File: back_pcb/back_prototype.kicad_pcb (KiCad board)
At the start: 2 copper layers, 40 x 100 mm, 82 parts, among them P1 EXPANSION_LEFT, P2 EXPANSION_BOTTOM, P3 EXPANSION_TOP, P4 USB_A, P5 AUDIO_CONN, P6 ATMEGA_HEADER, P7 EXPANSION_BOTTOM2, P8 JST, P9 USB_A, Q1 IRLML6401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

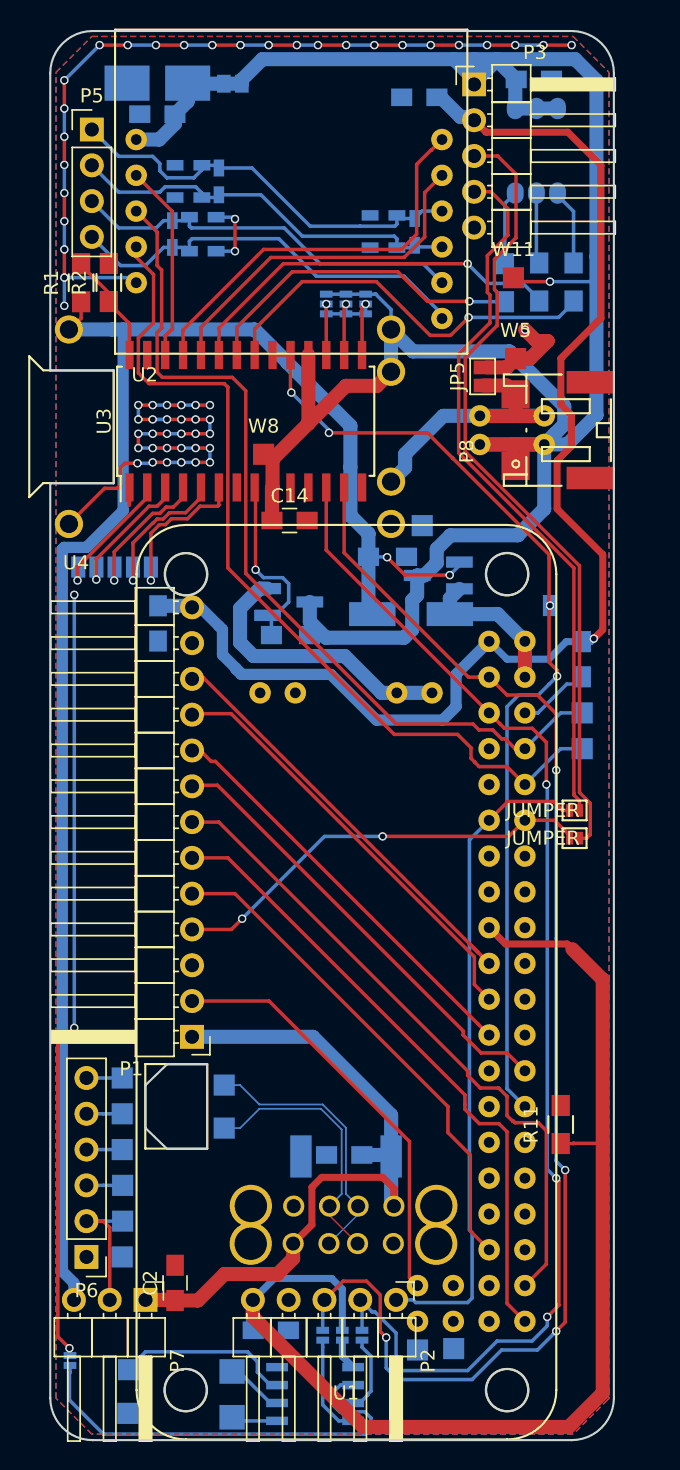
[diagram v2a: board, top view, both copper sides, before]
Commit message: Cleared up ground, removed testpoints
Removed some ground and I2C GPIO expander testpoints
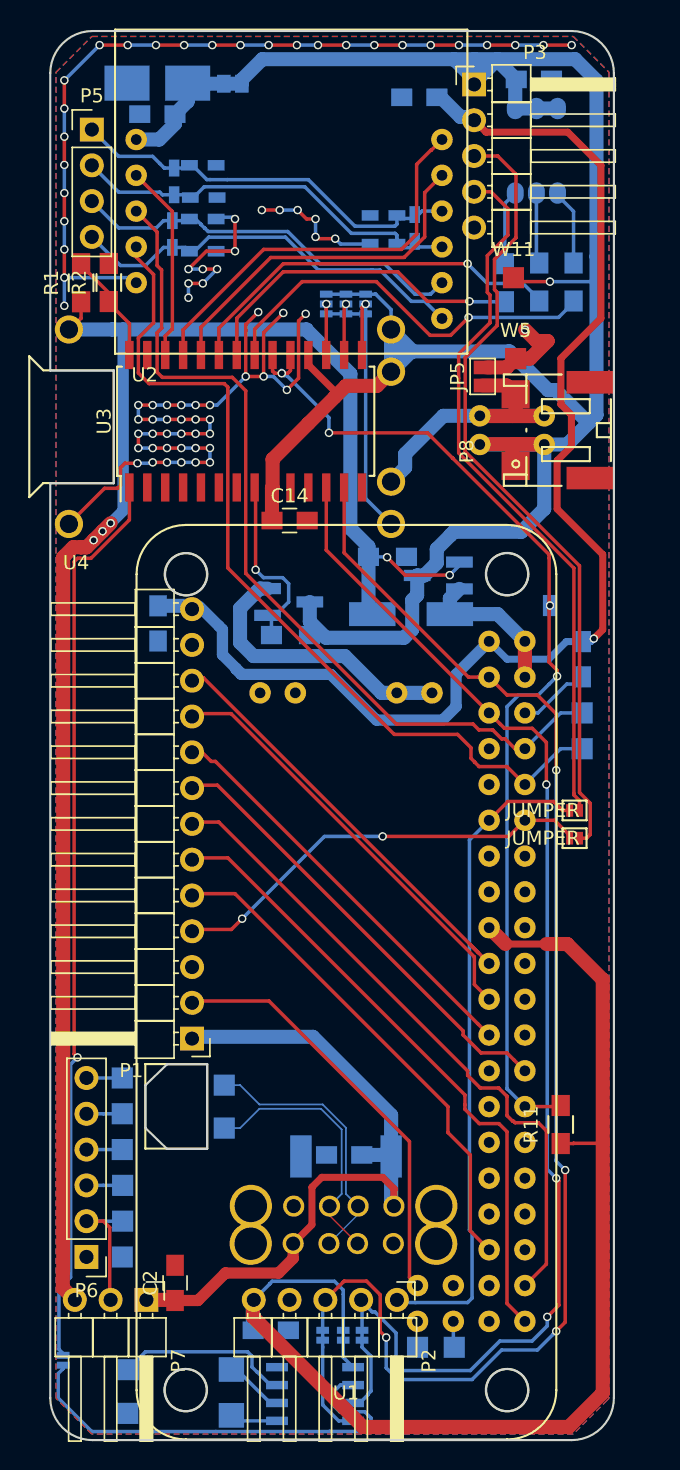
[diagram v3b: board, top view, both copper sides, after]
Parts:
- removed W12: GND, Measurement_Points:Measurement_Point_Square-SMD-Pad_Small
- removed W21, W22, W23, W24, W7, W8: TEST_1P, Measurement_Points:Measurement_Point_Square-SMD-Pad_Small
- moved C23 3.17 mm to (50.3, 50.7)
- moved C22 1.08 mm to (52.4, 51.8), turned to 180 degrees
- moved C24 1.02 mm to (52.3, 49.5), turned to 0 degrees
- moved JP2 0.48 mm to (42.4, 134.0)
- moved C17 0.28 mm to (67.4, 54.0)
- moved C16 0.25 mm to (65.2, 55.1)
- moved W4 0.19 mm to (67.6, 133.4)
- moved Y1 0.15 mm to (54.4, 136.6)
- moved C21 0.13 mm to (52.3, 53.3)
- moved P1 0.13 mm to (51.6, 111.5)
- moved W3 0.10 mm to (70.2, 133.4)
- moved JP7 0.06 mm to (62.3, 132.2)
- moved P7 0.06 mm to (48.3, 130.0)
- moved P2 0.06 mm to (66.1, 130.0)
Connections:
- JP10 pad 1: Net-(JP10-Pad1) -> SDA
- JP2 pad 1: Net-(JP2-Pad1) -> RTC_ALARM
- JP7 pad 1: Net-(JP7-Pad1) -> +3V3
- JP9 pad 1: Net-(JP9-Pad1) -> SCL
- U3 pad 2: Net-(U3-Pad2) -> (no net)
- U3 pad 3: Net-(U3-Pad3) -> (no net)
- U3 pad 4: Net-(U3-Pad4) -> (no net)
- U3 pad 5: Net-(U3-Pad5) -> (no net)
- U3 pad 6: Net-(U3-Pad6) -> (no net)
- U3 pad 7: Net-(U3-Pad7) -> (no net)
- U5 pad 5: Net-(JP7-Pad1) -> +3V3
- U5 pad 6: Net-(JP2-Pad1) -> RTC_ALARM
- U5 pad 7: Net-(JP9-Pad1) -> SCL
- U5 pad 8: Net-(JP10-Pad1) -> SDA
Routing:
- net GND: track 128.7 -> 185.7 mm, vias 63 -> 81
- net RTC_ALARM: track 56.1 -> 96.6 mm, vias 3 -> 1
- net Net-(JP2-Pad1): track 31.3 -> 0.00 mm
- net Net-(U3-Pad5): track 10.5 -> 0.00 mm, vias 1 -> 0
- net Net-(U3-Pad6): track 10.3 -> 0.00 mm, vias 1 -> 0
- net Net-(U3-Pad4): track 10.2 -> 0.00 mm, vias 1 -> 0
- net Net-(U3-Pad3): track 9.79 -> 0.00 mm, vias 1 -> 0
- net Net-(U3-Pad2): track 9.63 -> 0.00 mm, vias 1 -> 0
- net SDA: track 95.1 -> 103.4 mm
- net Net-(JP10-Pad1): track 7.70 -> 0.00 mm
- net +BATT: track 166.0 -> 173.2 mm
- net SCL: track 88.3 -> 94.1 mm
- net Net-(U3-Pad7): track 5.59 -> 0.00 mm
- net Net-(JP9-Pad1): track 5.52 -> 0.00 mm
- net MCP_INT: track 69.6 -> 74.4 mm
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
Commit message: Final changes
* Added fiducials
* Modified footprints to have bigger holes
* Added OSHW logo, release information and references
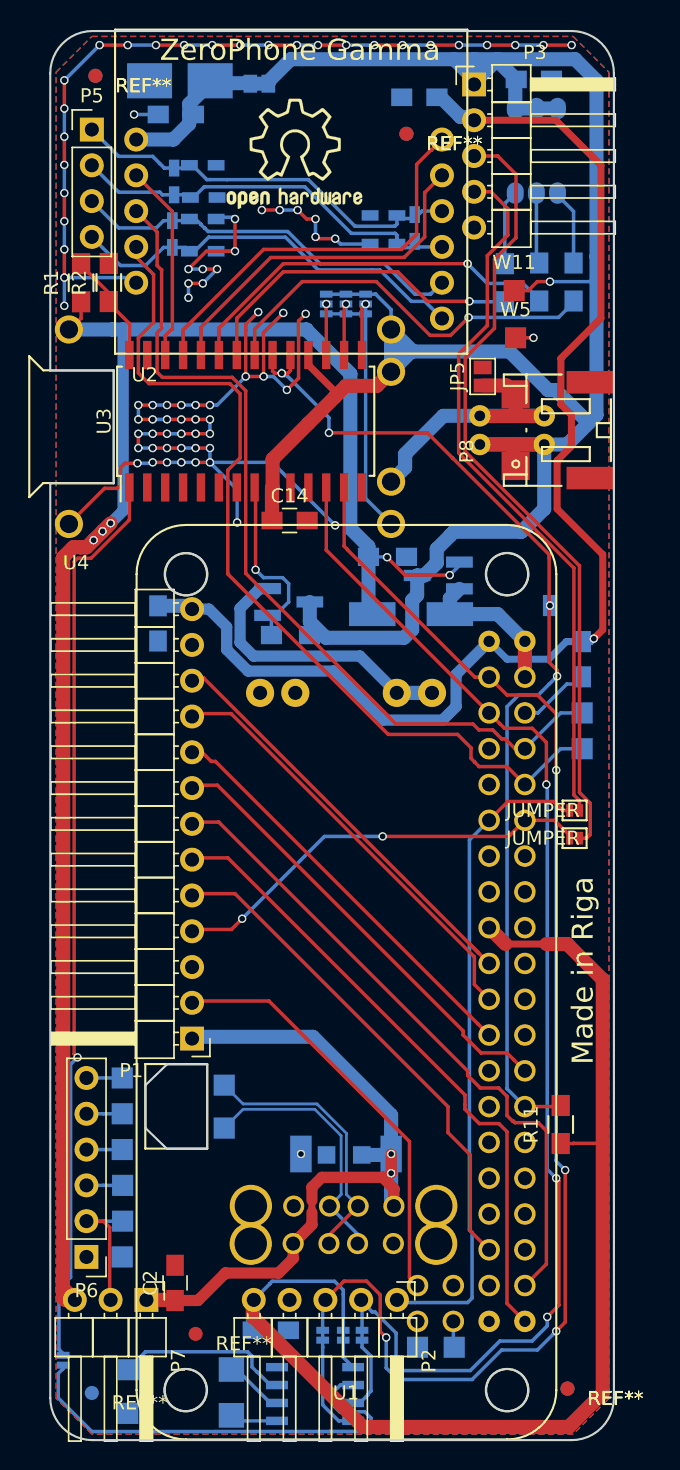
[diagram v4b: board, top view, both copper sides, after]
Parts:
- added G***: LOGO, art:oshw_logo_10x8mm, B.Cu at (58.9, 48.7)
- added G***: LOGO, art:oshw_logo_10x8mm, F.Cu at (58.8, 48.7)
- added REF**: Fiducial_1mm_Dia_2.54mm_Outer_CopperTop, Fiducials:Fiducial_1mm_Dia_2.54mm_Outer_CopperTop, F.Cu at (51.8, 132.5)
- added REF**: Fiducial_1mm_Dia_2.54mm_Outer_CopperTop, Fiducials:Fiducial_1mm_Dia_2.54mm_Outer_CopperTop, F.Cu at (78.2, 136.3)
- added REF**: Fiducial_1mm_Dia_2.54mm_Outer_CopperTop, Fiducials:Fiducial_1mm_Dia_2.54mm_Outer_CopperTop, F.Cu at (66.8, 47.3)
- added REF**: Fiducial_1mm_Dia_2.54mm_Outer_CopperTop, Fiducials:Fiducial_1mm_Dia_2.54mm_Outer_CopperTop, F.Cu at (44.7, 43.2)
- added REF**: Fiducial_1mm_Dia_2.54mm_Outer_CopperBottom, Fiducials:Fiducial_1mm_Dia_2.54mm_Outer_CopperBottom, F.Cu at (44.7, 43.2)
- added REF**: Fiducial_1mm_Dia_2.54mm_Outer_CopperBottom, Fiducials:Fiducial_1mm_Dia_2.54mm_Outer_CopperBottom, F.Cu at (66.8, 47.3)
- added REF**: Fiducial_1mm_Dia_2.54mm_Outer_CopperBottom, Fiducials:Fiducial_1mm_Dia_2.54mm_Outer_CopperBottom, F.Cu at (78.2, 136.3)
- added REF**: Fiducial_1mm_Dia_2.54mm_Outer_CopperBottom, Fiducials:Fiducial_1mm_Dia_2.54mm_Outer_CopperBottom, F.Cu at (44.5, 136.7)
- moved JP1 1.88 mm to (56.3, 43.7)
- moved C4 1.61 mm to (50.7, 43.5)
- moved W5 1.47 mm to (74.5, 61.8)
- moved C5 1.31 mm to (50.4, 45.9)
- moved W11 0.92 mm to (74.4, 58.4)
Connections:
- JP2 pad 1: RTC_ALARM -> Net-(JP2-Pad1)
- U5 pad 6: RTC_ALARM -> Net-(JP2-Pad1)
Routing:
- net RTC_ALARM: track 96.6 -> 64.5 mm
- net Net-(JP2-Pad1): track 0.00 -> 32.0 mm
- net GND: track 185.7 -> 197.5 mm, vias 81 -> 85
- net +5V: track 50.5 -> 52.5 mm, vias 0 -> 2
- net VDD: track 123.7 -> 125.5 mm
- net SIM800_TXD: track 62.5 -> 63.7 mm
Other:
- board text added: "Designed in KiCad"
- board text added: "Made in Riga"
- board text added: "ZeroPhone Gamma"

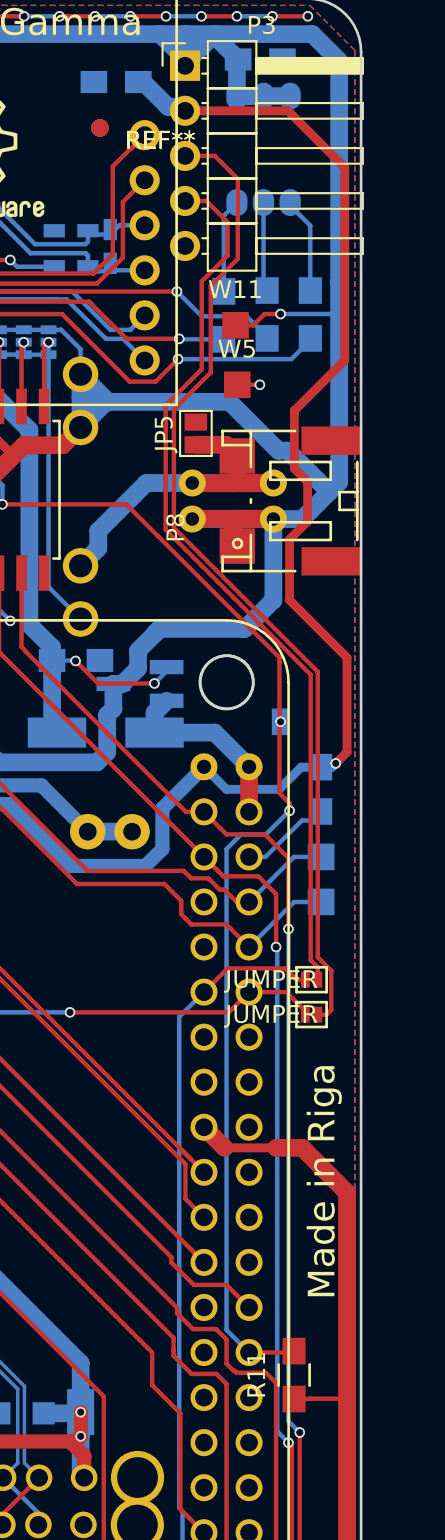
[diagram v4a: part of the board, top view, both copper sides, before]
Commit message: Minor back PCB changes
Moved some testpoints and a capacitor
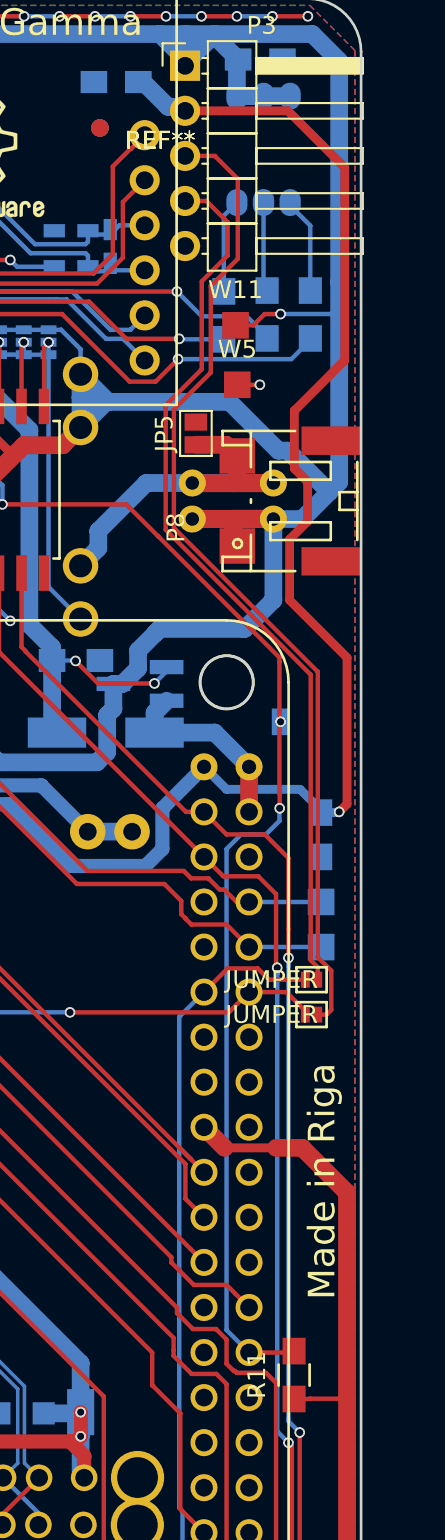
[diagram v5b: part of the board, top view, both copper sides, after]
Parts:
- moved C15 2.56 mm to (79.2, 87.1)
- moved W1 2.54 mm to (79.2, 90.9)
- moved W2 2.54 mm to (79.2, 93.5)
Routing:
- net GND: track 197.5 -> 192.6 mm
- net +3V3: track 178.5 -> 181.4 mm
- net SIM800_RXD: track 62.2 -> 61.1 mm
- net SIM800_TXD: track 63.7 -> 62.7 mm

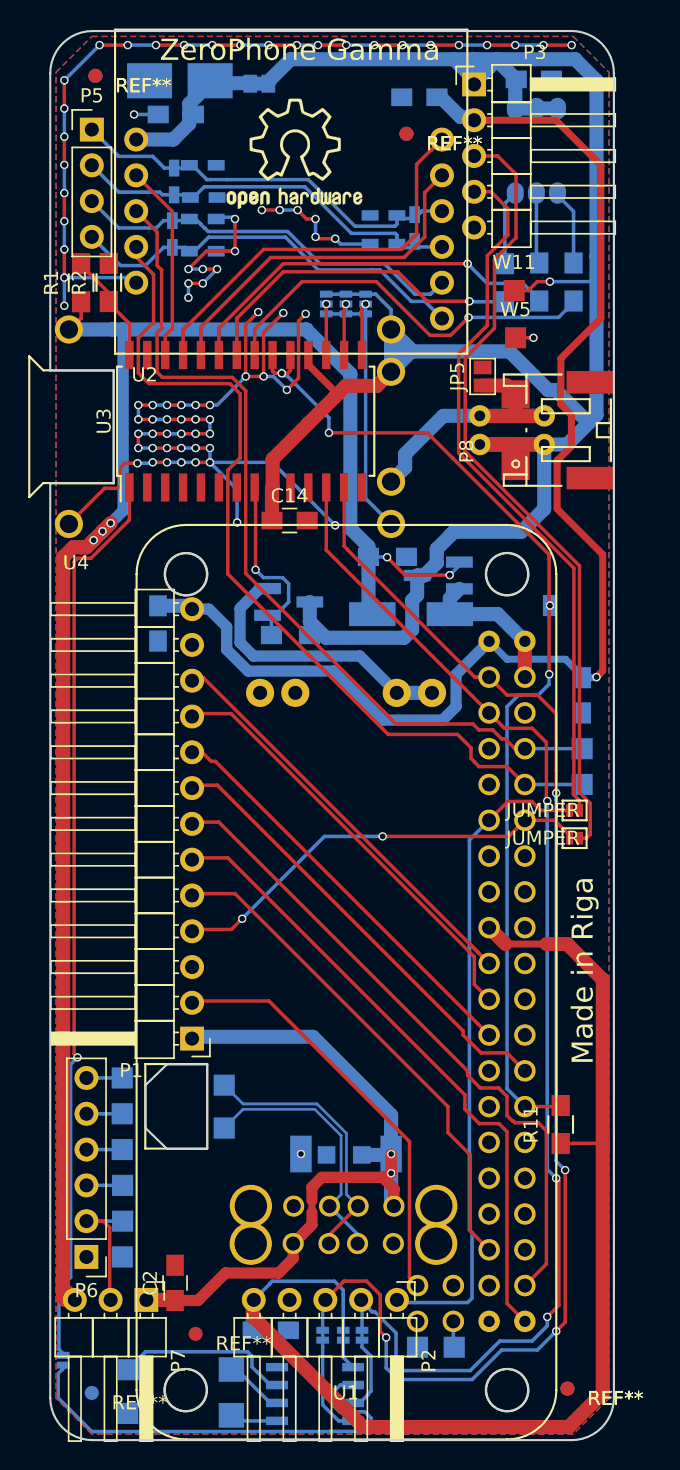
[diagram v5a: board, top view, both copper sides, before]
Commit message: Last minute changes in back board
* Added a VSYS capacitor
* Added a capacitor in parallel with the battery
* Removed the MCP_INT testpoint and testpoints for free MCP GPIOs
* Remove the footprint for additional protection IC
* Stitched the board with vias
* Moved the traces around for better grounds
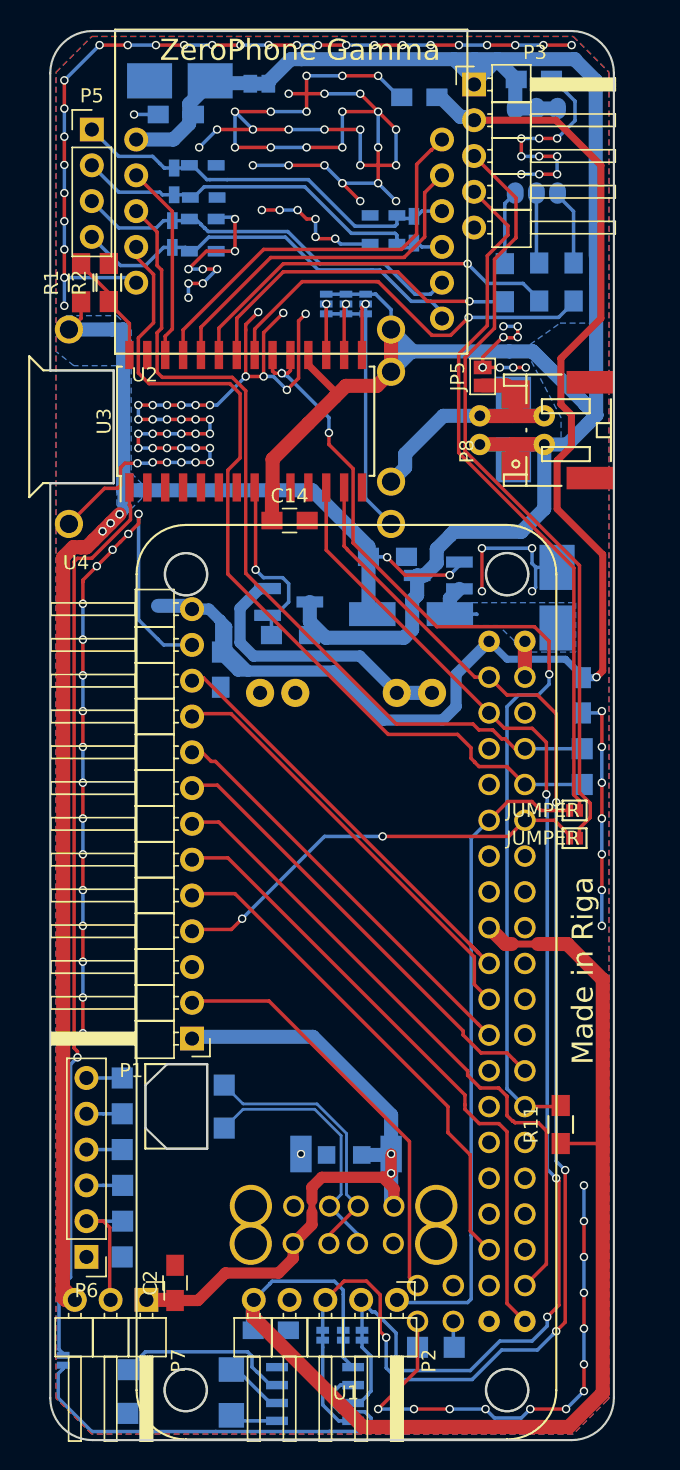
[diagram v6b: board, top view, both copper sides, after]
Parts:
- removed G*** (x2): LOGO, art:oshw_logo_10x8mm
- removed REF** (x4): Fiducial_1mm_Dia_2.54mm_Outer_CopperTop, Fiducials:Fiducial_1mm_Dia_2.54mm_Outer_CopperTop
- removed REF** (x4): Fiducial_1mm_Dia_2.54mm_Outer_CopperBottom, Fiducials:Fiducial_1mm_Dia_2.54mm_Outer_CopperBottom
- removed W11: BAT_IN, Measurement_Points:Measurement_Point_Square-SMD-Pad_Small
- removed W28: TEST_1P, Measurement_Points:Measurement_Point_Square-SMD-Pad_Small
- removed W5: GND, Measurement_Points:Measurement_Point_Square-SMD-Pad_Small
- added C3: 100uF, Capacitors_Tantalum_SMD:CP_Tantalum_Case-B_EIA-3528-21_Hand, B.Cu at (74.4, 68.3)
- added C7: 100uF, Capacitors_Tantalum_SMD:CP_Tantalum_Case-B_EIA-3528-21_Hand, B.Cu at (77.5, 80.2)
- moved C8 5.53 mm to (53.6, 85.3)
- moved C17 0.14 mm to (67.3, 54.1)
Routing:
- net GND: track 192.6 -> 394.8 mm, vias 85 -> 172
- net VDD: track 125.5 -> 114.4 mm
- net +BATT: track 172.9 -> 179.4 mm, vias 1 -> 0
- net +3V3: track 181.4 -> 186.3 mm
- net VPP: track 10.8 -> 6.64 mm
- net BATT-: track 19.9 -> 21.7 mm
- net IR_TX: track 56.4 -> 55.1 mm
- net IR_RX: track 50.6 -> 49.9 mm
- net MCP_INT: track 73.9 -> 73.6 mm, vias 4 -> 3
- added copper zone on B.Cu, net +BATT
- added copper zone on B.Cu, net VDD
- added copper zone on B.Cu, net VPP
